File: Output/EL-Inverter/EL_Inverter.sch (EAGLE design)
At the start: 11 parts, among them Q1 MMBT5088, Q2 MMBT5088, Q3 MMBT5088

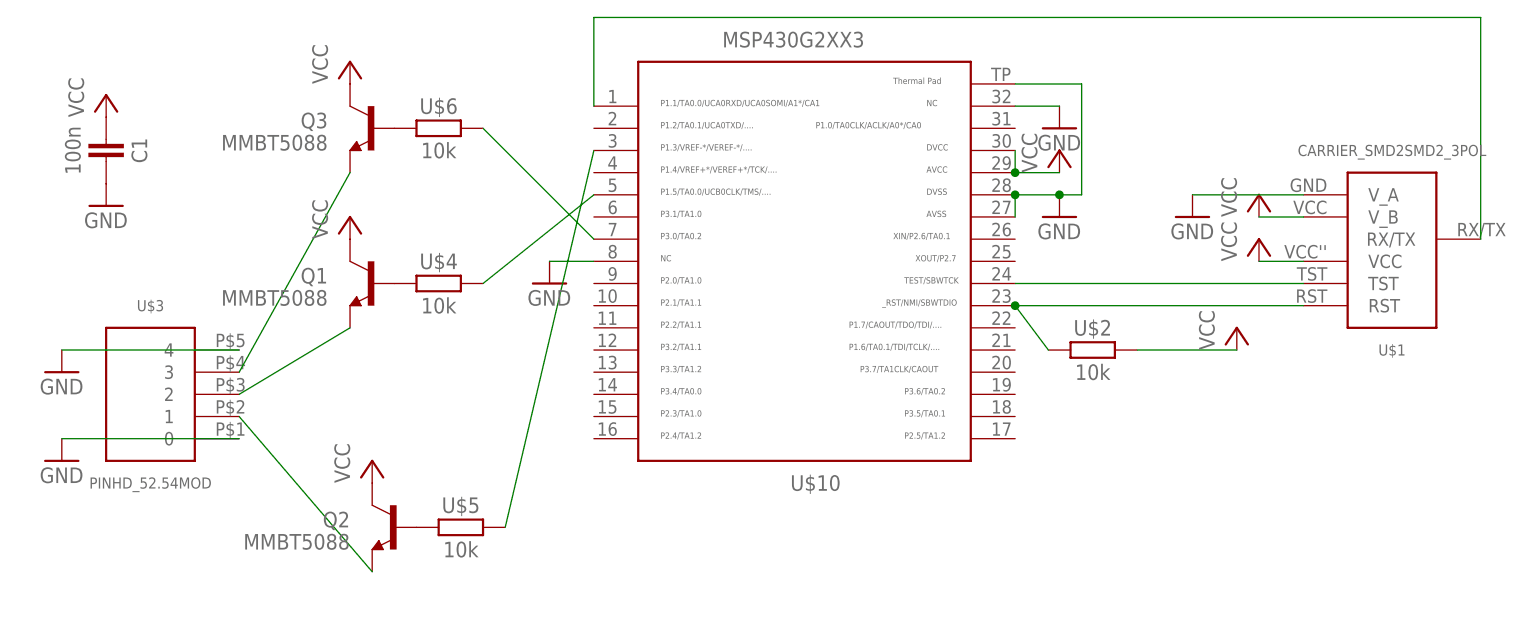
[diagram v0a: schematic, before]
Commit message: Update Pinheader
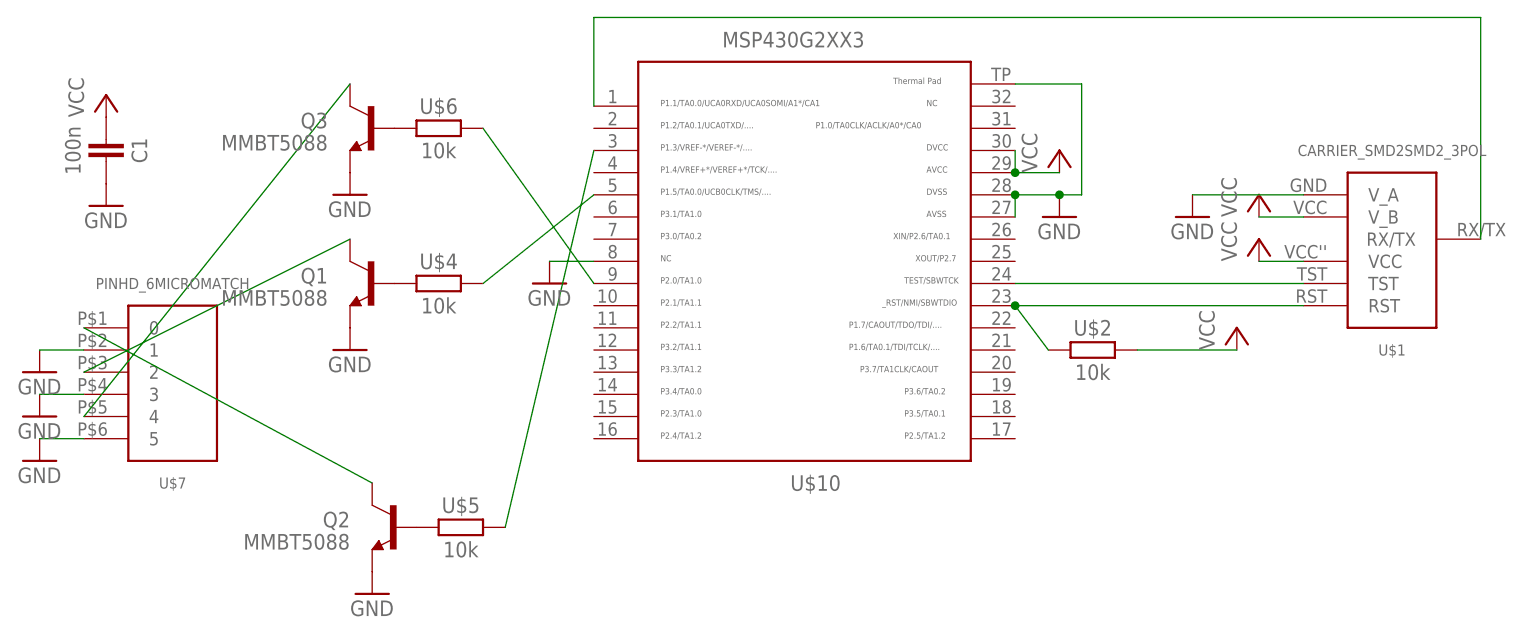
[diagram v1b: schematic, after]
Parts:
- removed U$3: PINHD_52.54MOD, thar:PINHD_52.54MOD
- added U$7: PINHD_6MICROMATCH, thar:PINHD_6MICROMATCH
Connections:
- net GND: now also Q1.E, Q2.E, Q3.E, U$7.1, U$7.3, U$7.5; no longer U$10.32, U$3.0, U$3.4
- net N$13: now also Q3.C, U$7.4; no longer Q3.E, U$3.3
- net N$17: now also U$10.9; no longer U$10.7
- net N$6: now also Q2.C, U$7.0; no longer Q2.E, U$3.1
- net N$7: now also Q1.C, U$7.2; no longer Q1.E, U$3.2
- net VCC: no longer Q1.C, Q2.C, Q3.C
